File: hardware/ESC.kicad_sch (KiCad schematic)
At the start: 1 part, among them U1 DRV8323HRTAR

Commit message: started schematic
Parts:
- removed U1: DRV8323HRTAR, RTA0040B, symbol ESC-Imports:DRV8323HRTAR
- added C1, C10, C11, C12, C13, C14, C15, C16, C17, C2, C3, C4, C5, C6, C7, C8, C9: C, symbol Device:C
- added C18, C19, C20, C21: 100uF, symbol Device:C
- added D1: D_Schottky, symbol Device:D_Schottky
- added D2: SMBJ30A, symbol Device:D_TVS
- added J1: +, symbol Connector_Generic:Conn_01x01
- added J2: -, symbol Connector_Generic:Conn_01x01
- added L1, L2: L, symbol Device:L
- added Q1, Q2, Q3, Q4, Q5, Q6, Q7: SIR426DP-T1-GE3, symbol Device:Q_NMOS
- added R1, R10, R11, R12, R2, R3, R4, R5, R6, R7, R8, R9: R, symbol Device:R
- added R13: 1K, symbol Device:R
- added U1: DRV8323RSRGZR, DRV8323RSRGZR:QFN50P700X700X100-49N, symbol ESC-Imports:DRV8323RSRGZR
- added U2: STM32G431CBTx, Package_QFP:LQFP-48_7x7mm_P0.5mm, symbol MCU_ST_STM32G4:STM32G431CBTx
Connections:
- new net: C19.1, C20.1, C21.1, L2.2
- new net: Q5.D, R8.1
- new net: C13.1, U1.36 (DVDD)
- new net: R11.1, R12.2, U1.1 (FB)
- new net: C11.1, U1.4 (CPH)
- new net: C11.2, U1.3 (CPL)
- new net: C18.1, L2.1, Q7.D
- new net: Q3.D, R5.1
- new net: C16.1, C4.2, Q4.S, R4.1
- new net: C4.1, R6.2
- new net: C15.1, C2.2, Q2.S, R3.1
- new net: C3.1, R5.2
- new net: C2.1, R2.2
- new net: D2.2 (A2), J1.1 (Pin_1), Q7.S
- new net: C5.1, R8.2
- new net: C12.1, U1.5 (VCP)
- new net: U2.23 (VSS), U2.35 (VSS), U2.47 (VSS)
- new net: C7.1, U1.44 (CB)
- new net: Q7.G, R13.1
- new net: R10.2, U1.48 (SHDN_N)
- new net: C6.1, R9.2
- new net: C17.1, C6.2, Q6.S, R7.1
- new net: Q1.D, R1.1
- new net: C1.1, R1.2
- new net +3.3V: C8.1, L1.2, R11.2, U1.26 (VREF)
- new net BGND: C7.2, D1.1 (K), L1.1, U1.45 (SW)
- new net GND: C10.2, C13.2, C14.2, C15.2, C16.2, C17.2, C18.2, C19.2, C20.2, C21.2, C8.2, C9.2, D1.2 (A), D2.1 (A1), J2.1 (Pin_1), R12.1, R13.2, R3.2, R4.2, R7.2, U1.2 (PGND), U1.27 (DGND), U1.35 (AGND), U1.43 (BGND)
- new net MISO: U1.29 (SDO)
- new net MOSI: U1.30 (SDI)
- new net MOTOR_A: C1.2, Q1.S, Q2.D, R2.1
- new net MOTOR_B: C3.2, Q3.S, Q4.D, R6.1
- new net MOTOR_C: C5.2, Q5.S, Q6.D, R9.1
- new net NSS: U1.32 (SCS_N)
- new net SCLK: U1.31 (SCLK)
- new net VBUS: C10.1, C12.2, C14.1, C9.1, R10.1, U1.47 (VIN), U1.6 (VM)

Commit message: finished most of schematic
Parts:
- removed L2: L, symbol Device:L
- removed Q7: SIR426DP-T1-GE3, symbol Device:Q_NMOS
- added C22, C23: 1nF, Capacitor_SMD:C_0603_1608Metric, symbol Device:C
- added C24, C33: 8.2pF, Capacitor_SMD:C_0402_1005Metric, symbol Device:C
- added C25, C32: 1nF, Capacitor_SMD:C_0402_1005Metric, symbol Device:C
- added C26, C27, C28, C30: 100nF, Capacitor_SMD:C_0402_1005Metric, symbol Device:C
- added C29: 1uF, Capacitor_SMD:C_0402_1005Metric, symbol Device:C
- added C31: 10uF, Capacitor_SMD:C_0402_1005Metric, symbol Device:C
- added FB1, FB2: FerriteBead, Inductor_SMD:L_0603_1608Metric, symbol Device:FerriteBead
- added J3, J7: Conn_01x03, Connector_PinHeader_2.54mm:PinHeader_1x03_P2.54mm_Vertical, symbol Connector_Generic:Conn_01x03
- added J4, J5, J6: +, Connector_Wire:SolderWire-4sqmm_1x01_D3mm_OD6mm, symbol Connector_Generic:Conn_01x01
- added JP1: SolderJumper_2_Open, Jumper:SolderJumper-2_P1.3mm_Open_RoundedPad1.0x1.5mm, symbol Jumper:SolderJumper_2_Open
- added Q7: NCE55P30K, Package_TO_SOT_SMD:TO-252-2, symbol Device:Q_PMOS
- added R14, R15: 10k, Resistor_SMD:R_0402_1005Metric, symbol Device:R
- added R16, R18, R21, R22, R24, R26, R27: 162K, Resistor_SMD:R_0402_1005Metric, symbol Device:R
- added R17, R19, R23, R25: 20K, Resistor_SMD:R_0402_1005Metric, symbol Device:R
- added R20: 1K, Resistor_SMD:R_0402_1005Metric, symbol Device:R
- added Y1: X322516MLB4SI, Crystal:Crystal_SMD_3225-4Pin_3.2x2.5mm, symbol Device:Crystal_GND24
- C1, C2, C3, C4, C5, C6: value C -> 10nF; footprint (none) -> Capacitor_SMD:C_0402_1005Metric
- C10, C7, C9: value C -> 100nF; footprint (none) -> Capacitor_SMD:C_0402_1005Metric
- C11: value C -> 47nF; footprint (none) -> Capacitor_SMD:C_0402_1005Metric
- C12, C13: value C -> 1uF; footprint (none) -> Capacitor_SMD:C_0402_1005Metric
- C14: value C -> 2.2uF; footprint (none) -> Capacitor_SMD:C_0402_1005Metric
- C15, C16, C17: value C -> 1nF; footprint (none) -> Capacitor_SMD:C_0402_1005Metric
- C18, C19, C20: footprint (none) -> Capacitor_SMD:C_Elec_6.3x7.7
- C21: value 100uF -> 100nF; footprint (none) -> Capacitor_SMD:C_0402_1005Metric
- C8: value C -> 10uF; footprint (none) -> Capacitor_SMD:C_0402_1005Metric
- D1: footprint (none) -> Diode_SMD:D_SOD-123
- D2: footprint (none) -> Diode_SMD:D_SMA
- J1, J2: footprint (none) -> Connector_Wire:SolderWire-4sqmm_1x01_D3mm_OD6mm
- L1: value L -> 22uH; footprint (none) -> Inductor_SMD:L_APV_ANR5012
- Q1, Q2, Q3, Q4, Q5, Q6: value SIR426DP-T1-GE3 -> AGM60P30AP; footprint (none) -> Package_DFN_QFN:PQFN-8-EP_6x5mm_P1.27mm_Generic
- R1, R2, R5, R6, R8, R9: value R -> 10; footprint (none) -> Resistor_SMD:R_0603_1608Metric
- R10: value R -> 100K; footprint (none) -> Resistor_SMD:R_0402_1005Metric
- R11: value R -> 3.3K; footprint (none) -> Resistor_SMD:R_0402_1005Metric
- R12: value R -> 1K; footprint (none) -> Resistor_SMD:R_0402_1005Metric
- R13: footprint (none) -> Resistor_SMD:R_0603_1608Metric
- R3, R4, R7: value R -> 1M; footprint (none) -> Resistor_SMD:R_1206_3216Metric
- U1: footprint DRV8323RSRGZR:QFN50P700X700X100-49N -> Package_DFN_QFN:QFN-48-1EP_7x7mm_P0.5mm_EP5.1x5.1mm_ThermalVias
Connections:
- net +3.3V: now also C21.1, U2.1 (VBAT), U2.24 (VDD), U2.36 (VDD), U2.48 (VDD), C26.1, C27.1, C28.1, C29.1, FB1.2, FB2.2, R14.2, R15.2, R20.2; no longer U1.26 (VREF)
- net GND: now also U1.12 (SNA), U1.13 (SNB), U1.22 (SNC), U2.19 (VSSA), U2.23 (VSS), U2.35 (VSS), U2.47 (VSS), C22.2, C23.2, C24.2, C25.2, C26.2, C27.2, C28.2, C29.2, C30.2, C31.2, C32.2, C33.2, J3.3 (Pin_3), J7.3 (Pin_3), R17.2, R19.2, R23.2, R25.2, Y1.2, Y1.4
- net MISO: now also U2.14 (PA6), R15.1
- net MOSI: now also U2.15 (PA7)
- net MOTOR_A: now also C3.2, C5.2, Q1.1 (S), Q2.3 (D), Q3.1 (S), Q4.3 (D), Q5.1 (S), Q6.3 (D), R6.1, R9.1, U1.9 (SHA), J4.1 (Pin_1), J5.1 (Pin_1), J6.1 (Pin_1), R16.1, R18.1, R22.1; no longer Q1.S, Q2.D
- net NSS: now also U2.12 (PA4)
- net VBUS: now also C18.1, C19.1, C20.1, Q1.3 (D), Q3.3 (D), Q5.3 (D), R1.1, R5.1, R8.1, U1.7 (VDRAIN), Q7.S, R24.1
- net SPB: now reaches C16.1, C4.2, R4.1
- net SPB: now also Q4.1 (S), U1.14 (SPB); no longer Q4.S
- net SPA: now reaches C15.1, C2.2, R3.1
- net SPA: now also Q2.1 (S), U1.11 (SPA); no longer Q2.S
- net at D2.2 (A2), J1.1 (Pin_1): now also Q7.D
- net BEMF_B: now reaches U2.10 (PA2)
- net BEMF_B: now also C22.1, R16.2, R17.1, R26.2
- net BEMF_C: now reaches U2.11 (PA3)
- net BEMF_C: now also C25.1, R22.2, R23.1, R27.2
- net SCK: now reaches U2.13 (PA5)
- net VIRTUAL_N: now reaches U2.16 (PB0)
- net VIRTUAL_N: now also R21.1, R26.1, R27.1
- net SOC: now reaches U2.17 (PB1)
- net SOC: now also U1.23 (SOC)
- net +3.3VA: now reaches U2.20 (VREF+)
- net +3.3VA: now also U2.21 (VDDA), C30.1, C31.1, FB2.1
- net SOB: now reaches U2.25 (PB11)
- net SOB: now also U1.24 (SOB)
- net SOA: now reaches U2.26 (PB12)
- net SOA: now also U1.25 (SOA)
- net INLC: now reaches U2.28 (PB14)
- net INLC: now also U1.42 (INLC)
- net INHC: now reaches U2.29 (PB15)
- net INHC: now also U1.41 (INHC)
- net INLB: now reaches U2.30 (PA8)
- net INLB: now also U1.40 (INLB)
- net INHB: now reaches U2.31 (PA9)
- net INHB: now also U1.39 (INHB)
- net INLA: now reaches U2.32 (PA10)
- net INLA: now also U1.38 (INLA)
- net INHA: now reaches U2.33 (PA11)
- net INHA: now also U1.37 (INHA)
- net SWDIO: now reaches U2.37 (PA13)
- net SWDIO: now also J3.2 (Pin_2)
- net SWCLK: now reaches U2.38 (PA14)
- net SWCLK: now also J3.1 (Pin_1)
- net PWM_IN: now reaches U2.39 (PA15)
- net PWM_IN: now also J7.1 (Pin_1)
- net DIR: now reaches U2.40 (PB3)
- net DIR: now also J7.2 (Pin_2), JP1.1 (A)
- net HSE_IN: now reaches U2.5 (PF0)
- net HSE_IN: now also C24.1, Y1.1
- net HSE_OUT: now reaches U2.6 (PF1)
- net HSE_OUT: now also C33.1, Y1.3
- net IN_ADC: now reaches U2.8 (PA0)
- net IN_ADC: now also C32.1, R24.2, R25.1
- net BEMF_A: now reaches U2.9 (PA1)
- net BEMF_A: now also C23.1, R18.2, R19.1, R21.2
- net at R13.1: now also Q7.G
- net GLA: now reaches U1.10 (GLA)
- net GLA: now also Q2.2 (G), Q4.2 (G), Q6.2 (G)
- net GLB: now reaches U1.15 (GLB)
- net SHB: now reaches U1.16 (SHB)
- net GHB: now reaches U1.17 (GHB)
- net GHC: now reaches U1.18 (GHC)
- net SHC: now reaches U1.19 (SHC)
- net GLC: now reaches U1.20 (GLC)
- net SPC: now reaches U1.21 (SPC)
- net SPC: now also C17.1, C6.2, Q6.1 (S), R7.1
- net FAULT: now reaches U1.28 (FAULT_N)
- net FAULT: now also R14.1
- net DRV_EN: now reaches U1.33 (ENABLE)
- net DRV_CAL: now reaches U1.34 (CAL)
- net GHA: now reaches U1.8 (GHA)
- net GHA: now also Q1.2 (G), Q3.2 (G), Q5.2 (G)
- removed net MOTOR_B: C3.2, Q3.S, Q4.D, R6.1
- removed net MOTOR_C: C5.2, Q5.S, Q6.D, R9.1
- new net: JP1.2 (B), R20.1
- new net: FB1.1, U1.26 (VREF)
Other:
- moved on the sheet: C1, C13, C15, C16, C17, C18, C19, C20, Q1, Q2, Q3, Q4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

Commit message: layout first draft
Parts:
- C14, C29, C8: footprint Capacitor_SMD:C_0402_1005Metric -> Capacitor_SMD:C_0603_1608Metric
- C22, C23: footprint Capacitor_SMD:C_0603_1608Metric -> Capacitor_SMD:C_0402_1005Metric
- Q7: value NCE55P30K -> AGM60P30A; footprint Package_TO_SOT_SMD:TO-252-2 -> Package_DFN_QFN:PQFN-8-EP_6x5mm_P1.27mm_Generic
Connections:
- net GHA: no longer Q3.2 (G), Q5.2 (G)
- net GHB: now also Q3.2 (G)
- net GHC: now also Q5.2 (G)
- net GLA: no longer Q4.2 (G), Q6.2 (G)
- net GLB: now also Q4.2 (G)
- net GLC: now also Q6.2 (G)
- net GND: now also U1.49 (EP)
- net MOTOR_A: no longer C3.2, C5.2, J5.1 (Pin_1), J6.1 (Pin_1), Q3.1 (S), Q4.3 (D), Q5.1 (S), Q6.3 (D), R16.1, R22.1, R6.1, R9.1
- net VBUS: now also Q7.1 (S); no longer Q7.S
- net at D2.2 (A2), J1.1 (Pin_1): now also Q7.3 (D); no longer Q7.D
- net at R13.1: now also Q7.2 (G); no longer Q7.G
- net SHB renamed MOTOR_B
- net MOTOR_B: now also C3.2, J5.1 (Pin_1), Q3.1 (S), Q4.3 (D), R16.1, R6.1
- net SHC renamed MOTOR_C
- net MOTOR_C: now also C5.2, J6.1 (Pin_1), Q5.1 (S), Q6.3 (D), R22.1, R9.1
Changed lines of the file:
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@@
 	(wire
 		(pts
+			(xy 251.46 132.08) (xy 251.46 134.62)
+		)
+		(stroke
+			(width 0)
+			(type default)
+		)
+	)
+	(wire
+		(pts
 			(xy 271.78 66.04) (xy 275.59 66.04)
 		)
@@
 	(wire
 		(pts
+			(xy 250.19 132.08) (xy 251.46 132.08)
+		)
+		(stroke
+			(width 0)
+			(type default)
+		)
+	)
+	(wire
+		(pts
 			(xy 110.49 165.1) (xy 118.11 165.1)
 		)
@@
 		)
 	)
-	(label "GLA"
+	(label "GLB"
 		(at 68.58 165.1 0)
 		(effects
@@
 		)
 	)
-	(label "GHA"
+	(label "GHB"
 		(at 68.58 144.78 0)
 		(effects
@@
 		)
 	)
-	(label "GHA"
+	(label "GHC"
 		(at 123.19 144.78 0)
 		(effects
@@
 		)
 	)
-	(label "SHA"
+	(label "SHB"
 		(at 68.58 154.94 0)
 		(effects
@@
 		)
 	)
-	(label "SHA"
+	(label "SHC"
 		(at 123.19 154.94 0)
 		(effects
@@
 		)
 	)
-	(label "GLA"
+	(label "GLC"
 		(at 123.19 165.1 0)
 		(effects
@@
 			)
 		)
-		(property "Footprint" "Capacitor_SMD:C_0402_1005Metric"
+		(property "Footprint" "Capacitor_SMD:C_0603_1608Metric"
 			(at 272.7452 33.02 0)
 			(effects
@@
 			)
 		)
-		(property "Footprint" "Capacitor_SMD:C_0402_1005Metric"
+		(property "Footprint" "Capacitor_SMD:C_0603_1608Metric"
 			(at 130.5052 30.48 0)
 			(effects
@@
 			)
 		)
-		(property "Footprint" "Capacitor_SMD:C_0603_1608Metric"
+		(property "Footprint" "Capacitor_SMD:C_0402_1005Metric"
 			(at 111.4552 173.99 0)
 			(effects
@@
 			)
 		)
-		(property "Footprint" "Capacitor_SMD:C_0402_1005Metric"
+		(property "Footprint" "Capacitor_SMD:C_0603_1608Metric"
 			(at 276.5552 74.93 0)
 			(effects
@@
 			)
 		)
-		(property "Value" "NCE55P30K"
+		(property "Value" "AGM60P30A"
 			(at 43.18 20.32 90)
 			(effects
@@
 			)
 		)
-		(property "Footprint" "Package_TO_SOT_SMD:TO-252-2"
+		(property "Footprint" "Package_DFN_QFN:PQFN-8-EP_6x5mm_P1.27mm_Generic"
 			(at 40.64 21.59 0)
 			(effects
@@
 			)
 		)
-		(pin "D"
+		(pin "1"
 		)
-		(pin "S"
+		(pin "3"
 		)
-		(pin "G"
+		(pin "2"
 		)
 		(instances
@@
 			)
 		)
-		(property "Footprint" "Capacitor_SMD:C_0603_1608Metric"
+		(property "Footprint" "Capacitor_SMD:C_0402_1005Metric"
 			(at 58.1152 173.99 0)
 			(effects

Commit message: started routing schematic
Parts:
- removed J3: Conn_01x03, Connector_PinHeader_2.54mm:PinHeader_1x03_P2.54mm_Vertical, symbol Connector_Generic:Conn_01x03
- added J3, J8, J9: +, Connector_Wire:SolderWirePad_1x01_SMD_2x4mm, symbol Connector_Generic:Conn_01x01
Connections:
- net GND: now also J9.1 (Pin_1)
- net SWCLK: now also J3.1 (Pin_1)
- net SWDIO: now also J8.1 (Pin_1)
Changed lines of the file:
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@@
 	(wire
 		(pts
-			(xy 29.21 92.71) (xy 29.21 91.44)
+			(xy 29.21 93.98) (xy 29.21 92.71)
 		)
 		(stroke
@@
 	(wire
 		(pts
-			(xy 27.94 86.36) (xy 35.56 86.36)
+			(xy 27.94 85.09) (xy 35.56 85.09)
 		)
 		(stroke
@@
 	(wire
 		(pts
-			(xy 29.21 91.44) (xy 27.94 91.44)
+			(xy 29.21 92.71) (xy 27.94 92.71)
 		)
 		(stroke
@@
 	)
 	(label "SWCLK"
-		(at 35.56 86.36 180)
+		(at 35.56 85.09 180)
 		(effects
 			(font
@@
 	)
 	(symbol
+		(lib_id "Connector_Generic:Conn_01x01")
+		(at 22.86 88.9 180)
+		(unit 1)
+		(exclude_from_sim no)
+		(in_bom yes)
+		(on_board yes)
+		(dnp no)
+		(property "Reference" "J8"
+			(at 20.32 88.9 0)
+			(effects
+				(font
+					(size 1.27 1.27)
+				)
+			)
+		)
+		(property "Value" "+"
+			(at 20.066 88.646 0)
+			(effects
+				(font
+					(size 2.54 2.54)
+				)
+				(hide yes)
+			)
+		)
+		(property "Footprint" "Connector_Wire:SolderWirePad_1x01_SMD_2x4mm"
+			(at 22.86 88.9 0)
+			(effects
+				(font
+					(size 1.27 1.27)
+				)
+				(hide yes)
+			)
+		)
+		(property "Datasheet" "~"
+			(at 22.86 88.9 0)
+			(effects
+				(font
+					(size 1.27 1.27)
+				)
+				(hide yes)
+			)
+		)
+		(property "Description" "Generic connector, single row, 01x01, script generated (kicad-library-utils/schlib/autogen/connector/)"
+			(at 22.86 88.9 0)
+			(effects
+				(font
+					(size 1.27 1.27)
+				)
+				(hide yes)
+			)
+		)
+		(pin "1"
+		)
+		(instances
+			(project "ESC"
+				(path "/4de1658d-a5e4-45f8-9b2f-349bf6ebe789"
+					(reference "J8")
+					(unit 1)
+				)
+			)
+		)
+	)
+	(symbol
 		(lib_id "Device:L")
 		(at 266.7 66.04 90)
@@
 	)
 	(symbol
-		(lib_id "Connector_Generic:Conn_01x03")
-		(at 22.86 88.9 0)
-		(mirror y)
-		(unit 1)
-		(exclude_from_sim no)
-		(in_bom yes)
-		(on_board yes)
-		(dnp no)
-		(property "Reference" "J3"
-			(at 22.86 84.074 0)
-			(effects
-				(font
-					(size 1.27 1.27)
-				)
-			)
-		)
-		(property "Value" "Conn_01x03"
-			(at 22.86 82.55 0)
-			(effects
-				(font
-					(size 1.27 1.27)
-				)
-				(hide yes)
-			)
-		)
-		(property "Footprint" "Connector_PinHeader_2.54mm:PinHeader_1x03_P2.54mm_Vertical"
-			(at 22.86 88.9 0)
-			(effects
-				(font
-					(size 1.27 1.27)
-				)
-				(hide yes)
-			)
-		)
-		(property "Datasheet" "~"
-			(at 22.86 88.9 0)
-			(effects
-				(font
-					(size 1.27 1.27)
-				)
-				(hide yes)
-			)
-		)
-		(property "Description" "Generic connector, single row, 01x03, script generated (kicad-library-utils/schlib/autogen/connector/)"
-			(at 22.86 88.9 0)
-			(effects
-				(font
-					(size 1.27 1.27)
-				)
-				(hide yes)
-			)
-		)
-		(pin "1"
-		)
-		(pin "2"
-		)
-		(pin "3"
-		)
-		(instances
-			(project "ESC"
-				(path "/4de1658d-a5e4-45f8-9b2f-349bf6ebe789"
-					(reference "J3")
-					(unit 1)
-				)
-			)
-		)
-	)
-	(symbol
 		(lib_id "Connector_Generic:Conn_01x01")
 		(at 22.86 102.87 180)
@@
 	(symbol
 		(lib_id "power:GND")
-		(at 29.21 92.71 0)
+		(at 29.21 93.98 0)
 		(unit 1)
 		(exclude_from_sim no)
@@
 		(dnp no)
 		(property "Reference" "#PWR047"
-			(at 29.21 99.06 0)
+			(at 29.21 100.33 0)
 			(effects
 				(font
@@
 		)
 		(property "Value" "GND"
-			(at 29.21 96.52 0)
+			(at 29.21 97.79 0)
 			(effects
 				(font
@@
 		)
 		(property "Footprint" ""
-			(at 29.21 92.71 0)
+			(at 29.21 93.98 0)
 			(effects
 				(font
@@
 		)
 		(property "Datasheet" ""
-			(at 29.21 92.71 0)
+			(at 29.21 93.98 0)
 			(effects
 				(font
@@
 		)
 		(property "Description" "Power symbol creates a global label with name \"GND\" , ground"
-			(at 29.21 92.71 0)
+			(at 29.21 93.98 0)
 			(effects
 				(font
@@
 	)
 	(symbol
+		(lib_id "Connector_Generic:Conn_01x01")
+		(at 22.86 92.71 180)
+		(unit 1)
+		(exclude_from_sim no)
+		(in_bom yes)
+		(on_board yes)
+		(dnp no)
+		(property "Reference" "J9"
+			(at 20.32 92.71 0)
+			(effects
+				(font
+					(size 1.27 1.27)
+				)
+			)
+		)
+		(property "Value" "+"
+			(at 20.066 92.456 0)
+			(effects
+				(font
+					(size 2.54 2.54)
+				)
+				(hide yes)
+			)
+		)
+		(property "Footprint" "Connector_Wire:SolderWirePad_1x01_SMD_2x4mm"
+			(at 22.86 92.71 0)
+			(effects
+				(font
+					(size 1.27 1.27)
+				)
+				(hide yes)
+			)
+		)
+		(property "Datasheet" "~"
+			(at 22.86 92.71 0)
+			(effects
+				(font
+					(size 1.27 1.27)
+				)
+				(hide yes)
+			)
+		)
+		(property "Description" "Generic connector, single row, 01x01, script generated (kicad-library-utils/schlib/autogen/connector/)"
+			(at 22.86 92.71 0)
+			(effects
+				(font
+					(size 1.27 1.27)
+				)
+				(hide yes)
+			)
+		)
+		(pin "1"
+		)
+		(instances
+			(project "ESC"
+				(path "/4de1658d-a5e4-45f8-9b2f-349bf6ebe789"
+					(reference "J9")
+					(unit 1)
+				)
+			)
+		)
+	)
+	(symbol
 		(lib_id "power:+3.3VA")
 		(at 187.96 29.21 0)
@@
 					(unit 1)
 				)
+			)
+		)
+	)
+	(symbol
+		(lib_id "Connector_Generic:Conn_01x01")
+		(at 22.86 85.09 180)
+		(unit 1)
+		(exclude_from_sim no)
+		(in_bom yes)
+		(on_board yes)
+		(dnp no)
+		(property "Reference" "J3"
+			(at 20.32 85.09 0)
+			(effects
+				(font
+					(size 1.27 1.27)
+				)
+			)
+		)
+		(property "Value" "+"
+			(at 20.066 84.836 0)
+			(effects
+				(font
+					(size 2.54 2.54)
+				)
+				(hide yes)
+			)
+		)
+		(property "Footprint" "Connector_Wire:SolderWirePad_1x01_SMD_2x4mm"
+			(at 22.86 85.09 0)
+			(effects
+				(font
+					(size 1.27 1.27)
+				)
+				(hide yes)
+			)
+		)
+		(property "Datasheet" "~"
+			(at 22.86 85.09 0)
+			(effects
+				(font
+					(size 1.27 1.27)
+				)
+				(hide yes)
+			)
+		)
+		(property "Description" "Generic connector, single row, 01x01, script generated (kicad-library-utils/schlib/autogen/connector/)"
+			(at 22.86 85.09 0)
+			(effects
+				(font
+					(size 1.27 1.27)
+				)
+				(hide yes)
+			)
+		)
+		(pin "1"
+		)
+		(instances
+			(project "ESC"
+				(path "/4de1658d-a5e4-45f8-9b2f-349bf6ebe789"
+					(reference "J3")
+					(unit 1)
+				)

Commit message: routing pcb
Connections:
- net SCLK is gone; now on net SCK: U1.31 (SCLK)
- no-connect marks 0 -> 12
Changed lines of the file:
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@@
 		(color 0 0 0 0)
 	)
+	(no_connect
+		(at 130.81 85.09)
+	)
+	(no_connect
+		(at 130.81 64.77)
+	)
+	(no_connect
+		(at 130.81 82.55)
+	)
+	(no_connect
+		(at 130.81 80.01)
+	)
+	(no_connect
+		(at 130.81 59.69)
+	)
+	(no_connect
+		(at 166.37 72.39)
+	)
+	(no_connect
+		(at 130.81 62.23)
+	)
+	(no_connect
+		(at 130.81 46.99)
+	)
+	(no_connect
+		(at 130.81 87.63)
+	)
+	(no_connect
+		(at 130.81 90.17)
+	)
+	(no_connect
+		(at 130.81 95.25)
+	)
+	(no_connect
+		(at 130.81 92.71)
+	)
 	(wire
 		(pts
@@
 		)
 	)
-	(label "SCLK"
+	(label "SCK"
 		(at 256.54 111.76 180)
 		(effects

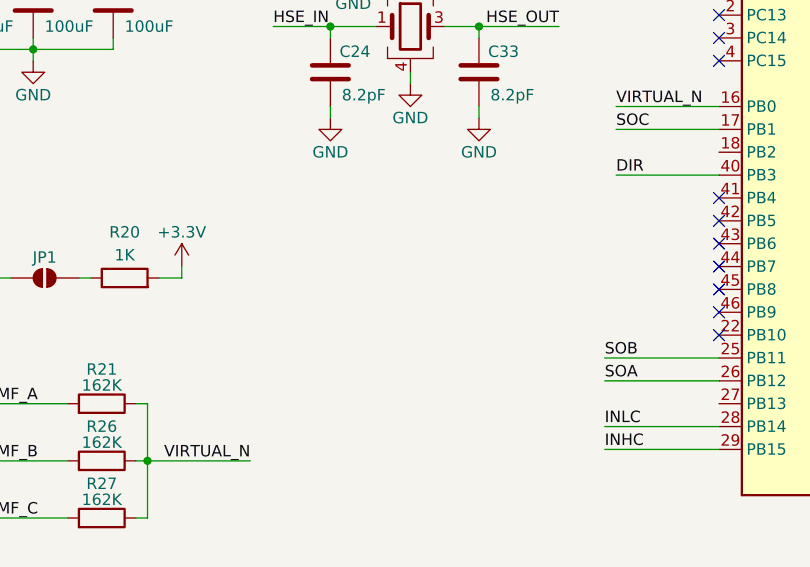
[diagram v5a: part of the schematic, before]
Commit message: updated to kicad 10.0
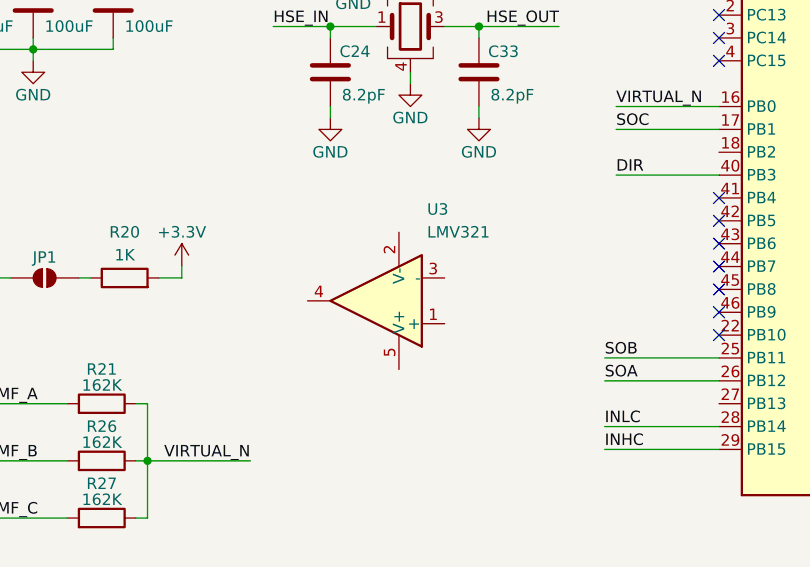
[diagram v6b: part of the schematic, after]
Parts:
- added U3: LMV321, Package_TO_SOT_SMD:SOT-23-5, symbol Amplifier_Operational:LMV321

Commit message: moved regulator
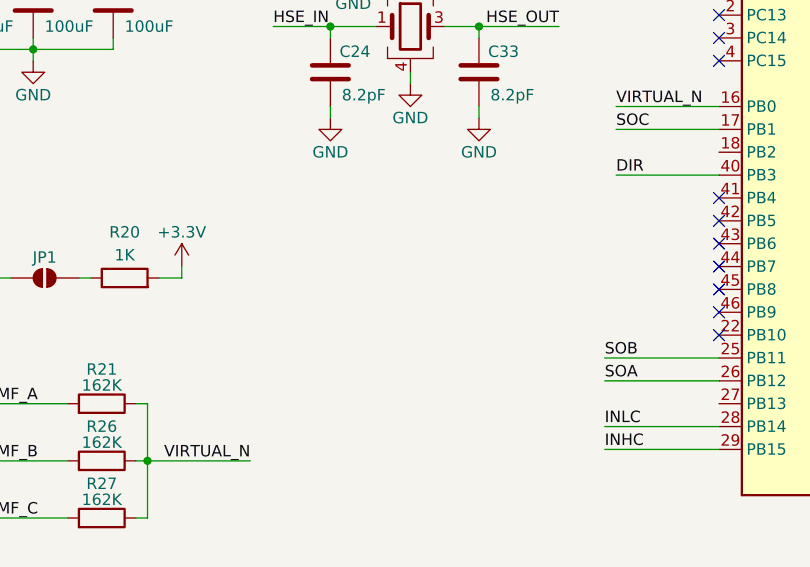
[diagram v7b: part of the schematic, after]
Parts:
- removed U3: LMV321, Package_TO_SOT_SMD:SOT-23-5, symbol Amplifier_Operational:LMV321
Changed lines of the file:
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@@
-	)
-	(symbol
-		(lib_id "Amplifier_Operational:LMV321")
-		(at 92.71 91.44 180)
-		(unit 1)
-		(body_style 1)
-		(exclude_from_sim no)
-		(in_bom yes)
-		(on_board yes)
-		(in_pos_files yes)
-		(dnp no)
-		(fields_autoplaced yes)
-		(property "Reference" "U3"
-			(at 98.3681 81.28 0)
-			(show_name no)
-			(do_not_autoplace no)
-			(effects
-				(font
-					(size 1.27 1.27)
-				)
-				(justify right)
-			)
-		)
-		(property "Value" "LMV321"
-			(at 98.3681 83.82 0)
-			(show_name no)
-			(do_not_autoplace no)
-			(effects
-				(font
-					(size 1.27 1.27)
-				)
-				(justify right)
-			)
-		)
-		(property "Footprint" "Package_TO_SOT_SMD:SOT-23-5"
-			(at 92.71 91.44 0)
-			(hide yes)
-			(show_name no)
-			(do_not_autoplace no)
-			(effects
-				(font
-					(size 1.27 1.27)
-				)
-				(justify left)
-			)
-		)
-		(property "Datasheet" "http://www.ti.com/lit/ds/symlink/lmv324.pdf"
-			(at 92.71 91.44 0)
-			(hide yes)
-			(show_name no)
-			(do_not_autoplace no)
-			(effects
-				(font
-					(size 1.27 1.27)
-				)
-			)
-		)
-		(property "Description" "Low-Voltage Rail-to-Rail Output Operational Amplifiers, SOT-23-5/SC-70-5"
-			(at 92.71 91.44 0)
-			(hide yes)
-			(show_name no)
-			(do_not_autoplace no)
-			(effects
-				(font
-					(size 1.27 1.27)
-				)
-			)
-		)
-		(pin "3"
-		)
-		(pin "2"
-		)
-		(pin "5"
-		)
-		(pin "1"
-		)
-		(pin "4"
-		)
-		(instances
-			(project "ESC"
-				(path "/4de1658d-a5e4-45f8-9b2f-349bf6ebe789"
-					(reference "U3")
-					(unit 1)
-				)
-			)
-		)
 	)
 	(symbol
